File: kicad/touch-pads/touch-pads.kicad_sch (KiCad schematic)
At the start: 19 parts, among them J1 Conn_01x06_Socket, J2 Conn_01x06_Socket, K1 Conn_01x01, K2 Conn_01x01, K3 Conn_01x01, K4 Conn_01x01, K5 Conn_01x01, K6 Conn_01x01, K7 Conn_01x01, K8 Conn_01x01, U1 CAP1188-1-CP-TR

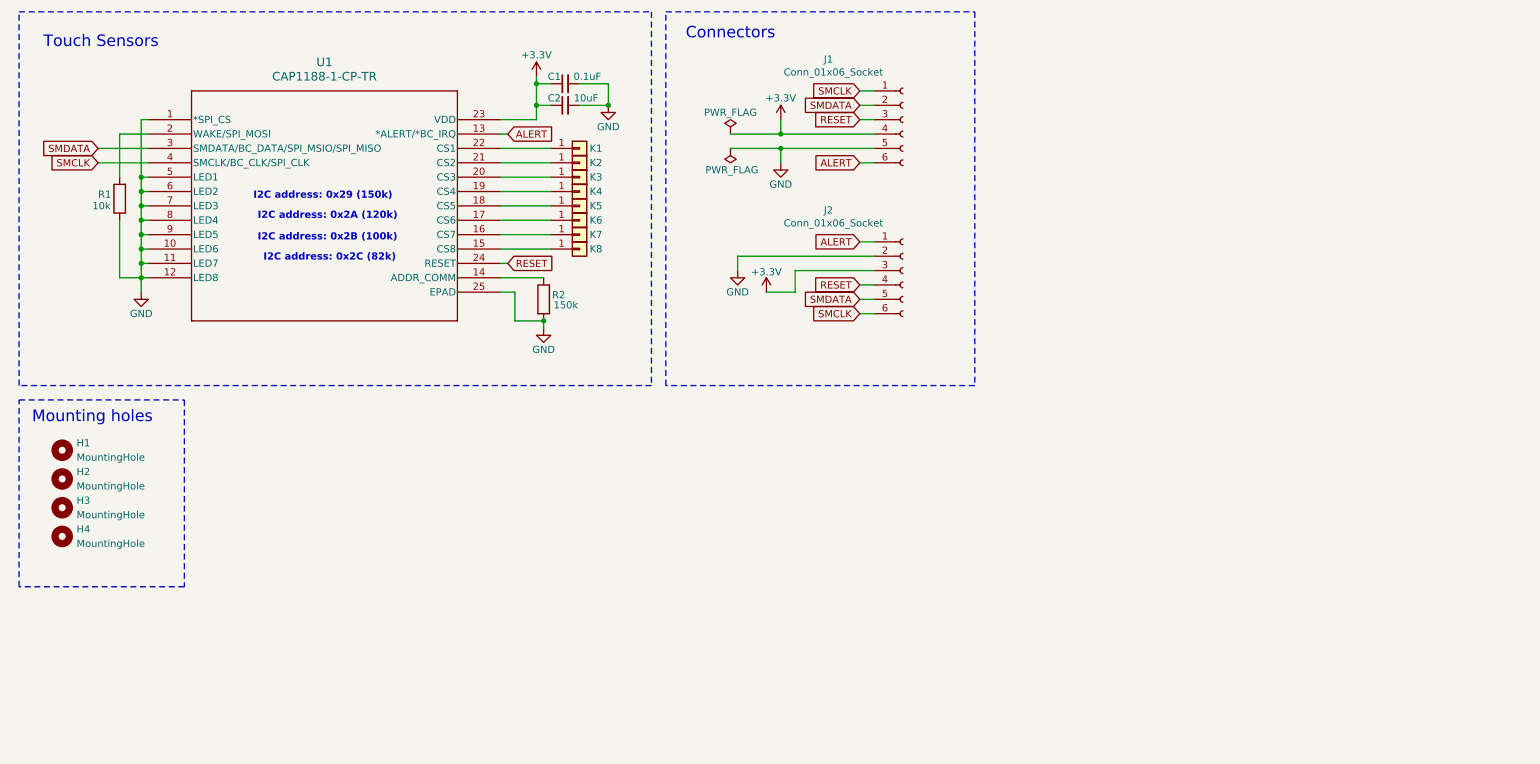
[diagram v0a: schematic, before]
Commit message: update touch pad
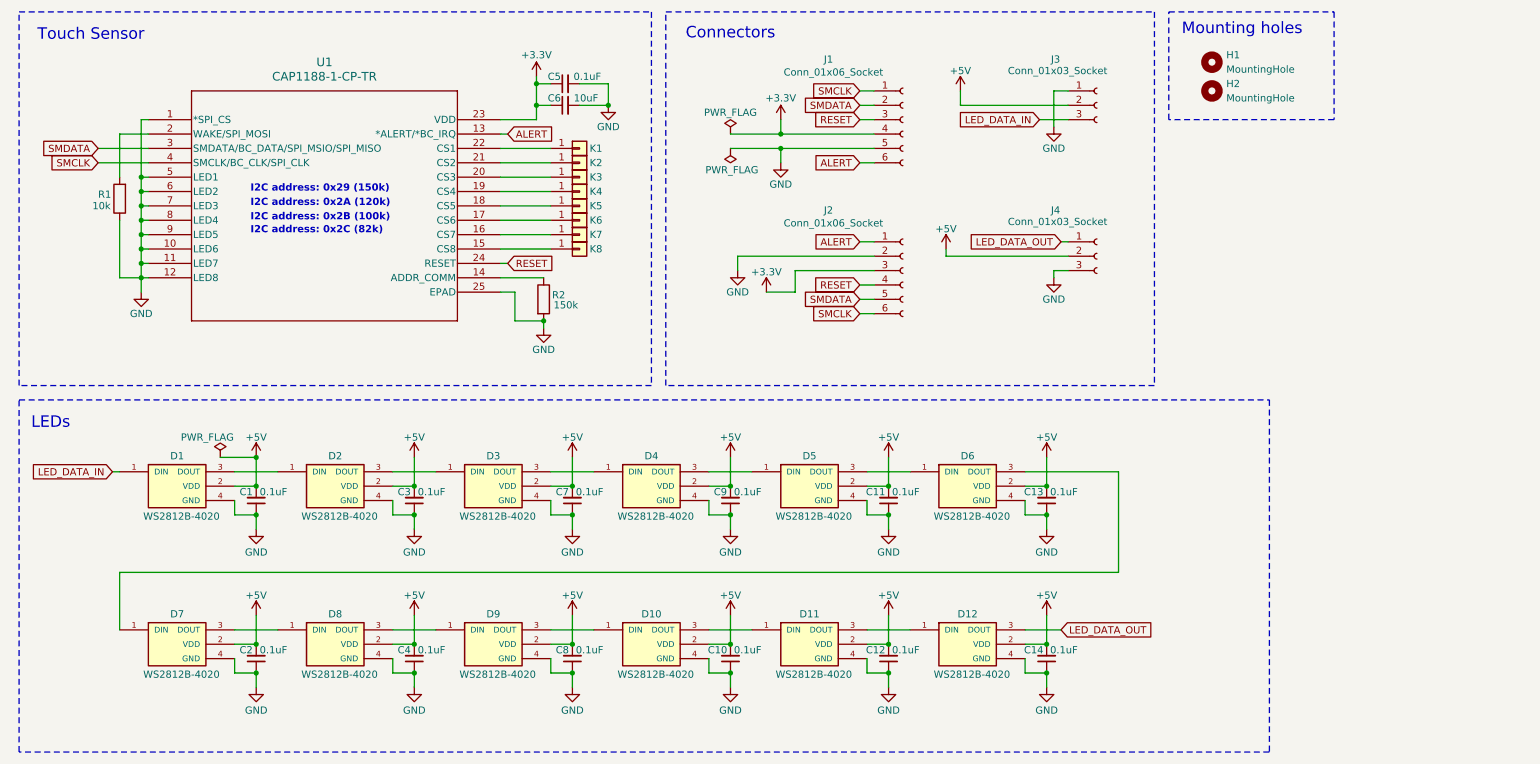
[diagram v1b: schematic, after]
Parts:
- removed H3, H4: MountingHole, MountingHole:MountingHole_3.2mm_M3, symbol Mechanical:MountingHole
- added C1, C10, C11, C12, C13, C14, C2, C3, C4, C7, C8, C9: 0.1uF, Capacitor_SMD:C_0805_2012Metric_Pad1.18x1.45mm_HandSolder, symbol Device:C_Small
- added D1, D10, D11, D12, D2, D3, D4, D5, D6, D7, D8, D9: WS2812B-4020, WS2812B-4020:WS2812B-4020, symbol WS2812B-4020:WS2812B-4020
- added J3, J4: Conn_01x03_Socket, Connector_JST:JST_PH_S3B-PH-SM4-TB_1x03-1MP_P2.00mm_Horizontal, symbol Connector:Conn_01x03_Socket
- renumbered C1 to C5, C2 to C6
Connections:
- net GND: now also C1.1, C10.1, C11.1, C12.1, C13.1, C14.1, C2.1, C3.1, C4.1, C7.1, C8.1, C9.1, D1.4 (GND), D10.4 (GND), D11.4 (GND), D12.4 (GND), D2.4 (GND), D3.4 (GND), D4.4 (GND), D5.4 (GND), D6.4 (GND), D7.4 (GND), D8.4 (GND), D9.4 (GND), J3.1 (Pin_1), J4.3 (Pin_3)
- new net: D5.3 (DOUT), D6.1 (DIN)
- new net: D6.3 (DOUT), D7.1 (DIN)
- new net: D1.3 (DOUT), D2.1 (DIN)
- new net: D11.3 (DOUT), D12.1 (DIN)
- new net: D7.3 (DOUT), D8.1 (DIN)
- new net: D8.3 (DOUT), D9.1 (DIN)
- new net: D3.3 (DOUT), D4.1 (DIN)
- new net: D4.3 (DOUT), D5.1 (DIN)
- new net: D10.1 (DIN), D9.3 (DOUT)
- new net: D2.3 (DOUT), D3.1 (DIN)
- new net: D10.3 (DOUT), D11.1 (DIN)
- new net +5V: C1.2, C10.2, C11.2, C12.2, C13.2, C14.2, C2.2, C3.2, C4.2, C7.2, C8.2, C9.2, D1.2 (VDD), D10.2 (VDD), D11.2 (VDD), D12.2 (VDD), D2.2 (VDD), D3.2 (VDD), D4.2 (VDD), D5.2 (VDD), D6.2 (VDD), D7.2 (VDD), D8.2 (VDD), D9.2 (VDD), J3.2 (Pin_2), J4.2 (Pin_2)
- new net LED_DATA_IN: D1.1 (DIN), J3.3 (Pin_3)
- new net LED_DATA_OUT: D12.3 (DOUT), J4.1 (Pin_1)
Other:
- note added: "LEDs"
- note added: "Touch Sensor"
- note removed: "Touch Sensors"
- moved on the sheet: H1, H2

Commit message: v3 touchpads with Tof sensors
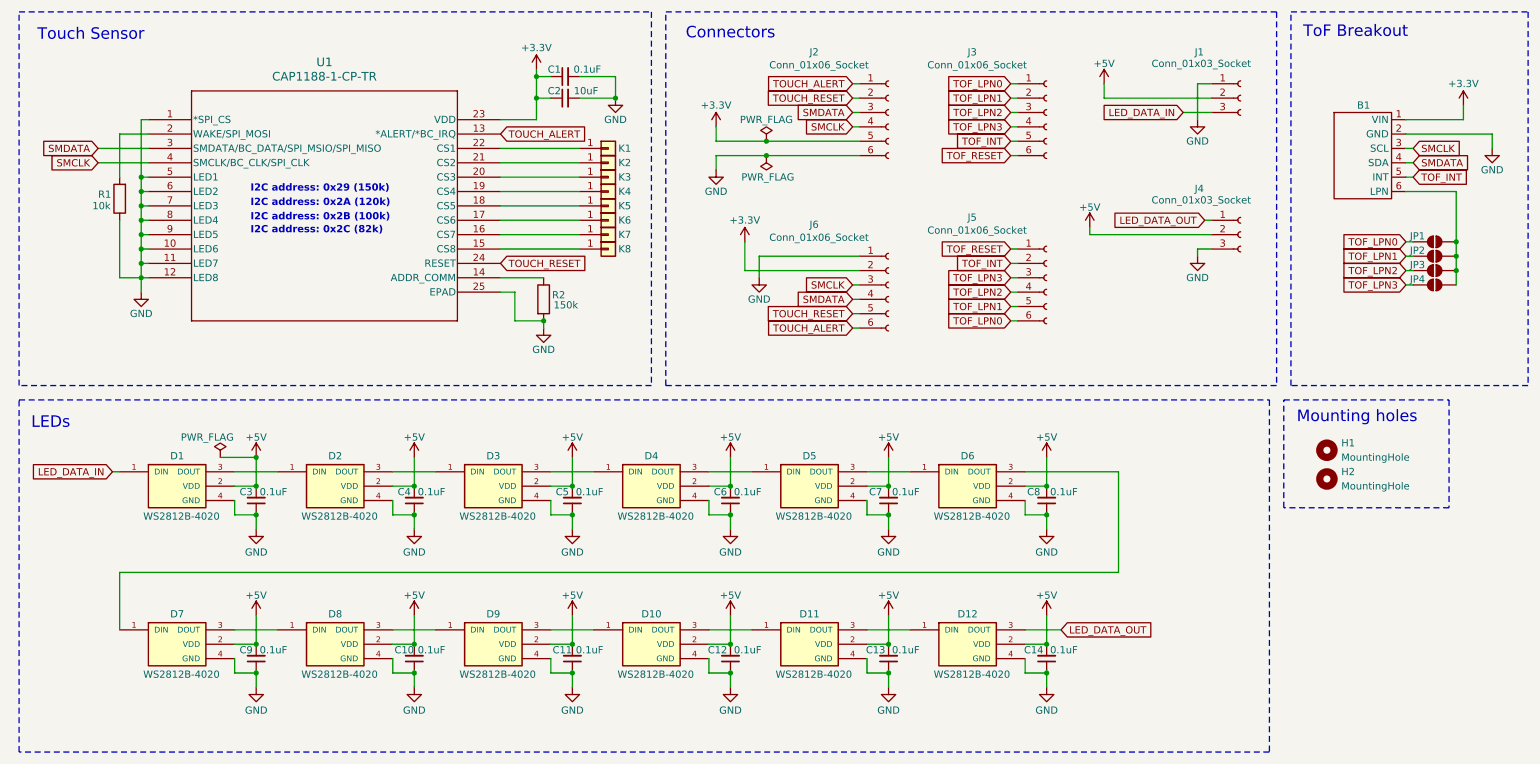
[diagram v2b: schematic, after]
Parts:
- removed J2: Conn_01x06_Socket, Connector_JST:JST_GH_SM06B-GHS-TB_1x06-1MP_P1.25mm_Horizontal, symbol Connector:Conn_01x06_Socket
- added B1: ~, VL53L5CX_Breakout:VL53L5CX_Breakout_Aliexpress, symbol VL53L5CX_Breakout:VL53L5CX_Breakout.pretty
- added J3, J5, J6: Conn_01x06_Socket, Connector_JST:JST_GH_SM06B-GHS-TB_1x06-1MP_P1.25mm_Horizontal, symbol Connector:Conn_01x06_Socket
- added JP1, JP2, JP3, JP4: SolderJumper_2_Open, Jumper:SolderJumper-2_P1.3mm_Open_RoundedPad1.0x1.5mm, symbol Jumper:SolderJumper_2_Open
- renumbered C5 to C1, C4 to C10, C8 to C11, C10 to C12, C12 to C13, C6 to C2, C1 to C3, C3 to C4, C7 to C5, C9 to C6, C11 to C7, C13 to C8, C2 to C9, J3 to J1, J1 to J2
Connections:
- net +3.3V: now also J2.5 (Pin_5), B1.1 (VIN), J6.2 (Pin_2); no longer J2.4 (Pin_4)
- net GND: now also J2.6 (Pin_6), B1.2 (GND), J6.1 (Pin_1); no longer J2.5 (Pin_5)
- net SMCLK: now also J2.4 (Pin_4), B1.3 (SCL), J6.3 (Pin_3); no longer J2.1 (Pin_1)
- net SMDATA: now also J2.3 (Pin_3), B1.4 (SDA), J6.4 (Pin_4); no longer J2.2 (Pin_2)
- net ALERT renamed TOUCH_ALERT
- net TOUCH_ALERT: now also J2.1 (Pin_1), J6.6 (Pin_6); no longer J2.6 (Pin_6)
- net RESET renamed TOUCH_RESET
- net TOUCH_RESET: now also J2.2 (Pin_2), J6.5 (Pin_5); no longer J2.3 (Pin_3)
- new net: B1.6 (LPN), JP1.2 (B), JP2.2 (B), JP3.2 (B), JP4.2 (B)
- new net TOF_INT: B1.5 (INT), J3.5 (Pin_5), J5.2 (Pin_2)
- new net TOF_LPN0: J3.1 (Pin_1), J5.6 (Pin_6), JP1.1 (A)
- new net TOF_LPN1: J3.2 (Pin_2), J5.5 (Pin_5), JP2.1 (A)
- new net TOF_LPN2: J3.3 (Pin_3), J5.4 (Pin_4), JP3.1 (A)
- new net TOF_LPN3: J3.4 (Pin_4), J5.3 (Pin_3), JP4.1 (A)
- new net TOF_RESET: J3.6 (Pin_6), J5.1 (Pin_1)
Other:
- note added: "ToF Breakout"
- moved on the sheet: C1, C2, H1, H2, J1, J2, J4, K1, K2, K3, K4, K5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

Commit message: update to kicad 9
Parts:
- B1: symbol VL53L5CX_Breakout:VL53L5CX_Breakout.pretty -> VL53L5CX_Breakout:VL53L5CX_Breakout
- D1, D10, D11, D12, D2, D3, D4, D5, D6, D7, D8, D9: footprint WS2812B-4020:WS2812B-4020 -> WS2812B-4020:LED_WS2812B-4020

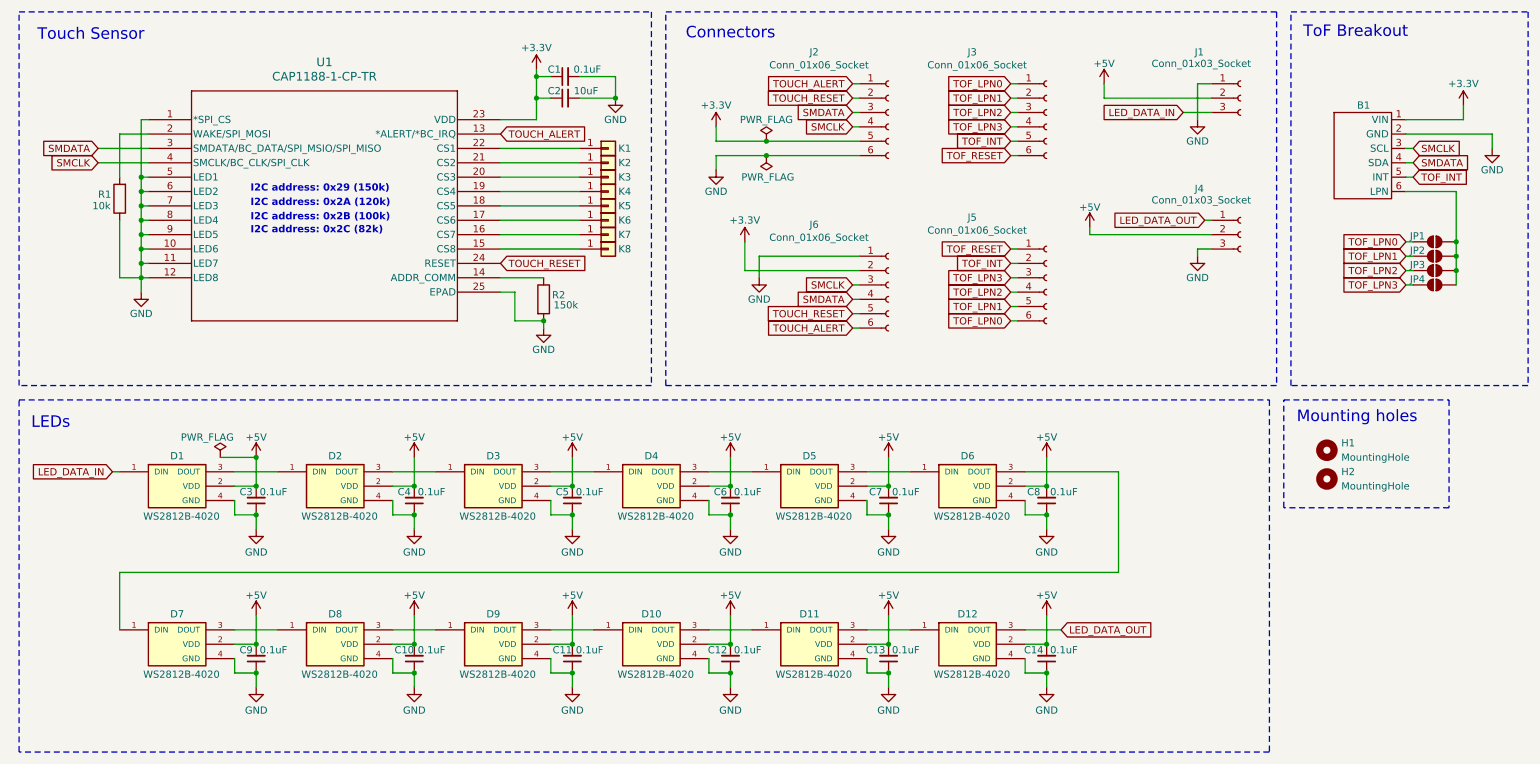
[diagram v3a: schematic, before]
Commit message: add mount holes
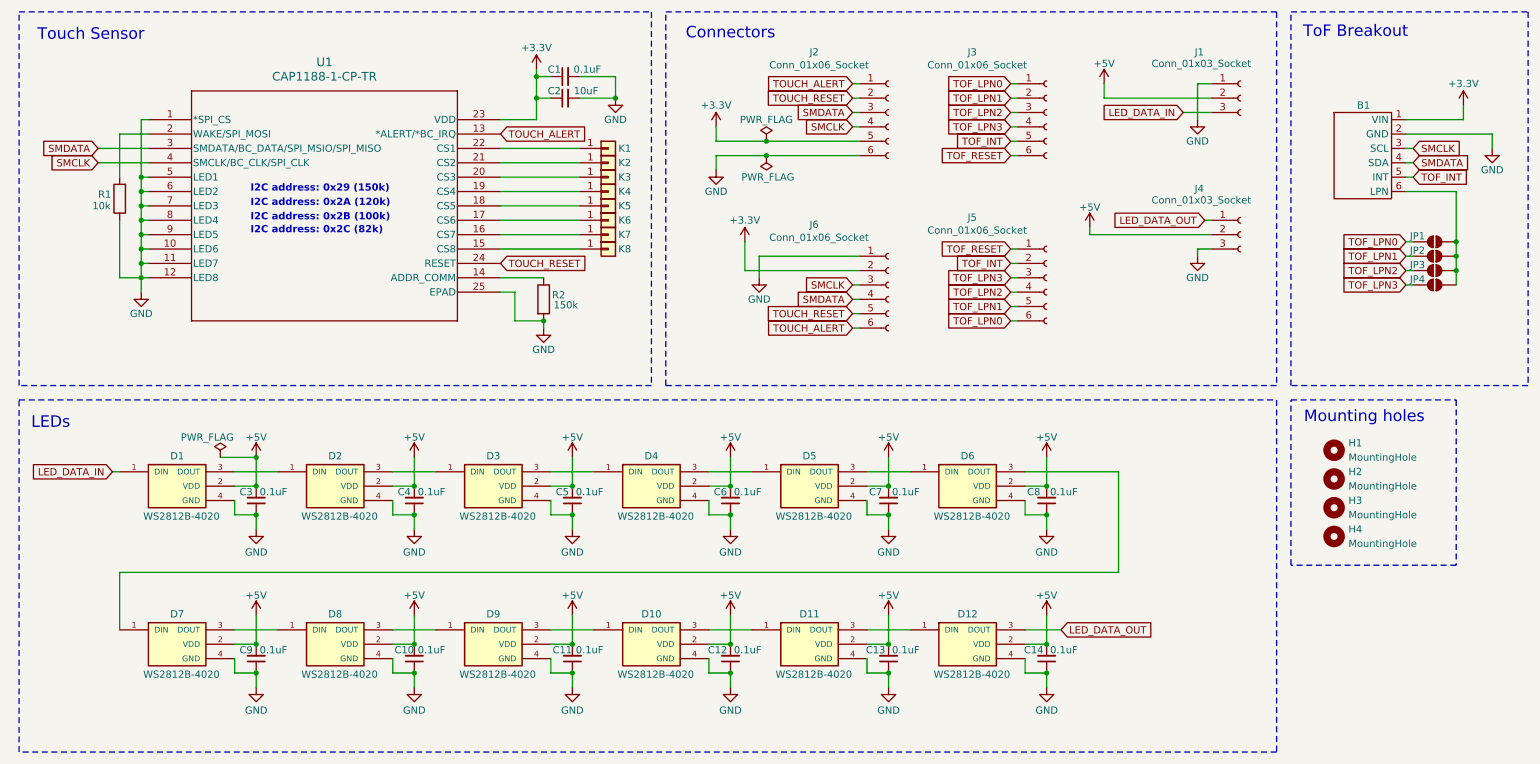
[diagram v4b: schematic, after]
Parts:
- added H3, H4: MountingHole, MountingHole:MountingHole_3.2mm_M3, symbol Mechanical:MountingHole
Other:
- moved on the sheet: H1, H2
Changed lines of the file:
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@@
 	)
 	(rectangle
-		(start 238.76 83.82)
-		(end 267.97 102.87)
+		(start 240.03 83.82)
+		(end 269.24 113.03)
 		(stroke
 			(width 0.2032)
@@
 	(rectangle
 		(start 15.24 83.82)
-		(end 236.22 146.05)
+		(end 237.49 146.05)
 		(stroke
 			(width 0.2032)
@@
 	(text "Mounting holes"
 		(exclude_from_sim no)
-		(at 251.714 86.868 0)
+		(at 252.984 86.868 0)
 		(effects
 			(font
@@
 	(symbol
 		(lib_id "Mechanical:MountingHole")
-		(at 246.38 92.71 0)
+		(at 247.65 92.71 0)
 		(unit 1)
 		(exclude_from_sim no)
@@
 		(fields_autoplaced yes)
 		(property "Reference" "H1"
-			(at 248.92 91.4399 0)
+			(at 250.19 91.4399 0)
 			(effects
 				(font
@@
 		)
 		(property "Value" "MountingHole"
-			(at 248.92 93.9799 0)
+			(at 250.19 93.9799 0)
 			(effects
 				(font
@@
 		)
 		(property "Footprint" "MountingHole:MountingHole_3.2mm_M3"
-			(at 246.38 92.71 0)
+			(at 247.65 92.71 0)
 			(effects
 				(font
@@
 		)
 		(property "Datasheet" "~"
-			(at 246.38 92.71 0)
+			(at 247.65 92.71 0)
 			(effects
 				(font
@@
 		)
 		(property "Description" "Mounting Hole without connection"
-			(at 246.38 92.71 0)
+			(at 247.65 92.71 0)
 			(effects
 				(font
@@
 	(symbol
 		(lib_id "Mechanical:MountingHole")
-		(at 246.38 97.79 0)
+		(at 247.65 97.79 0)
 		(unit 1)
 		(exclude_from_sim no)
@@
 		(fields_autoplaced yes)
 		(property "Reference" "H2"
-			(at 248.92 96.5199 0)
+			(at 250.19 96.5199 0)
 			(effects
 				(font
@@
 		)
 		(property "Value" "MountingHole"
-			(at 248.92 99.0599 0)
+			(at 250.19 99.0599 0)
 			(effects
 				(font
@@
 		)
 		(property "Footprint" "MountingHole:MountingHole_3.2mm_M3"
-			(at 246.38 97.79 0)
+			(at 247.65 97.79 0)
 			(effects
 				(font
@@
 		)
 		(property "Datasheet" "~"
-			(at 246.38 97.79 0)
+			(at 247.65 97.79 0)
 			(effects
 				(font
@@
 		)
 		(property "Description" "Mounting Hole without connection"
-			(at 246.38 97.79 0)
+			(at 247.65 97.79 0)
 			(effects
 				(font
@@
 	)
 	(symbol
+		(lib_id "Mechanical:MountingHole")
+		(at 247.65 102.87 0)
+		(unit 1)
+		(exclude_from_sim no)
+		(in_bom no)
+		(on_board yes)
+		(dnp no)
+		(fields_autoplaced yes)
+		(property "Reference" "H3"
+			(at 250.19 101.5999 0)
+			(effects
+				(font
+					(size 1.27 1.27)
+				)
+				(justify left)
+			)
+		)
+		(property "Value" "MountingHole"
+			(at 250.19 104.1399 0)
+			(effects
+				(font
+					(size 1.27 1.27)
+				)
+				(justify left)
+			)
+		)
+		(property "Footprint" "MountingHole:MountingHole_3.2mm_M3"
+			(at 247.65 102.87 0)
+			(effects
+				(font
+					(size 1.27 1.27)
+				)
+				(hide yes)
+			)
+		)
+		(property "Datasheet" "~"
+			(at 247.65 102.87 0)
+			(effects
+				(font
+					(size 1.27 1.27)
+				)
+				(hide yes)
+			)
+		)
+		(property "Description" "Mounting Hole without connection"
+			(at 247.65 102.87 0)
+			(effects
+				(font
+					(size 1.27 1.27)
+				)
+				(hide yes)
+			)
+		)
+		(instances
+			(project "touch-pads"
+				(path "/208e6366-7d11-4576-9309-e3e3af46f0ad"
+					(reference "H3")
+					(unit 1)
+				)
+			)
+		)
+	)
+	(symbol
 		(lib_id "power:GND")
 		(at 140.97 134.62 0)
@@
 					(unit 1)
 				)
+			)
+		)
+	)
+	(symbol
+		(lib_id "Mechanical:MountingHole")
+		(at 247.65 107.95 0)
+		(unit 1)
+		(exclude_from_sim no)
+		(in_bom no)
+		(on_board yes)
+		(dnp no)
+		(fields_autoplaced yes)
+		(property "Reference" "H4"
+			(at 250.19 106.6799 0)
+			(effects
+				(font
+					(size 1.27 1.27)
+				)
+				(justify left)
+			)
+		)
+		(property "Value" "MountingHole"
+			(at 250.19 109.2199 0)
+			(effects
+				(font
+					(size 1.27 1.27)
+				)
+				(justify left)
+			)
+		)
+		(property "Footprint" "MountingHole:MountingHole_3.2mm_M3"
+			(at 247.65 107.95 0)
+			(effects
+				(font
+					(size 1.27 1.27)
+				)
+				(hide yes)
+			)
+		)
+		(property "Datasheet" "~"
+			(at 247.65 107.95 0)
+			(effects
+				(font
+					(size 1.27 1.27)
+				)
+				(hide yes)
+			)
+		)
+		(property "Description" "Mounting Hole without connection"
+			(at 247.65 107.95 0)
+			(effects
+				(font
+					(size 1.27 1.27)
+				)
+				(hide yes)
+			)
+		)
+		(instances
+			(project "touch-pads"
+				(path "/208e6366-7d11-4576-9309-e3e3af46f0ad"
+					(reference "H4")
+					(unit 1)
+				)
